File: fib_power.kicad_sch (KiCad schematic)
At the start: 36 parts, among them U201 TLV75718PDBV, U202 TLV75733PDBV, U204 TPS56428DDA, U205 TPS56428DDA

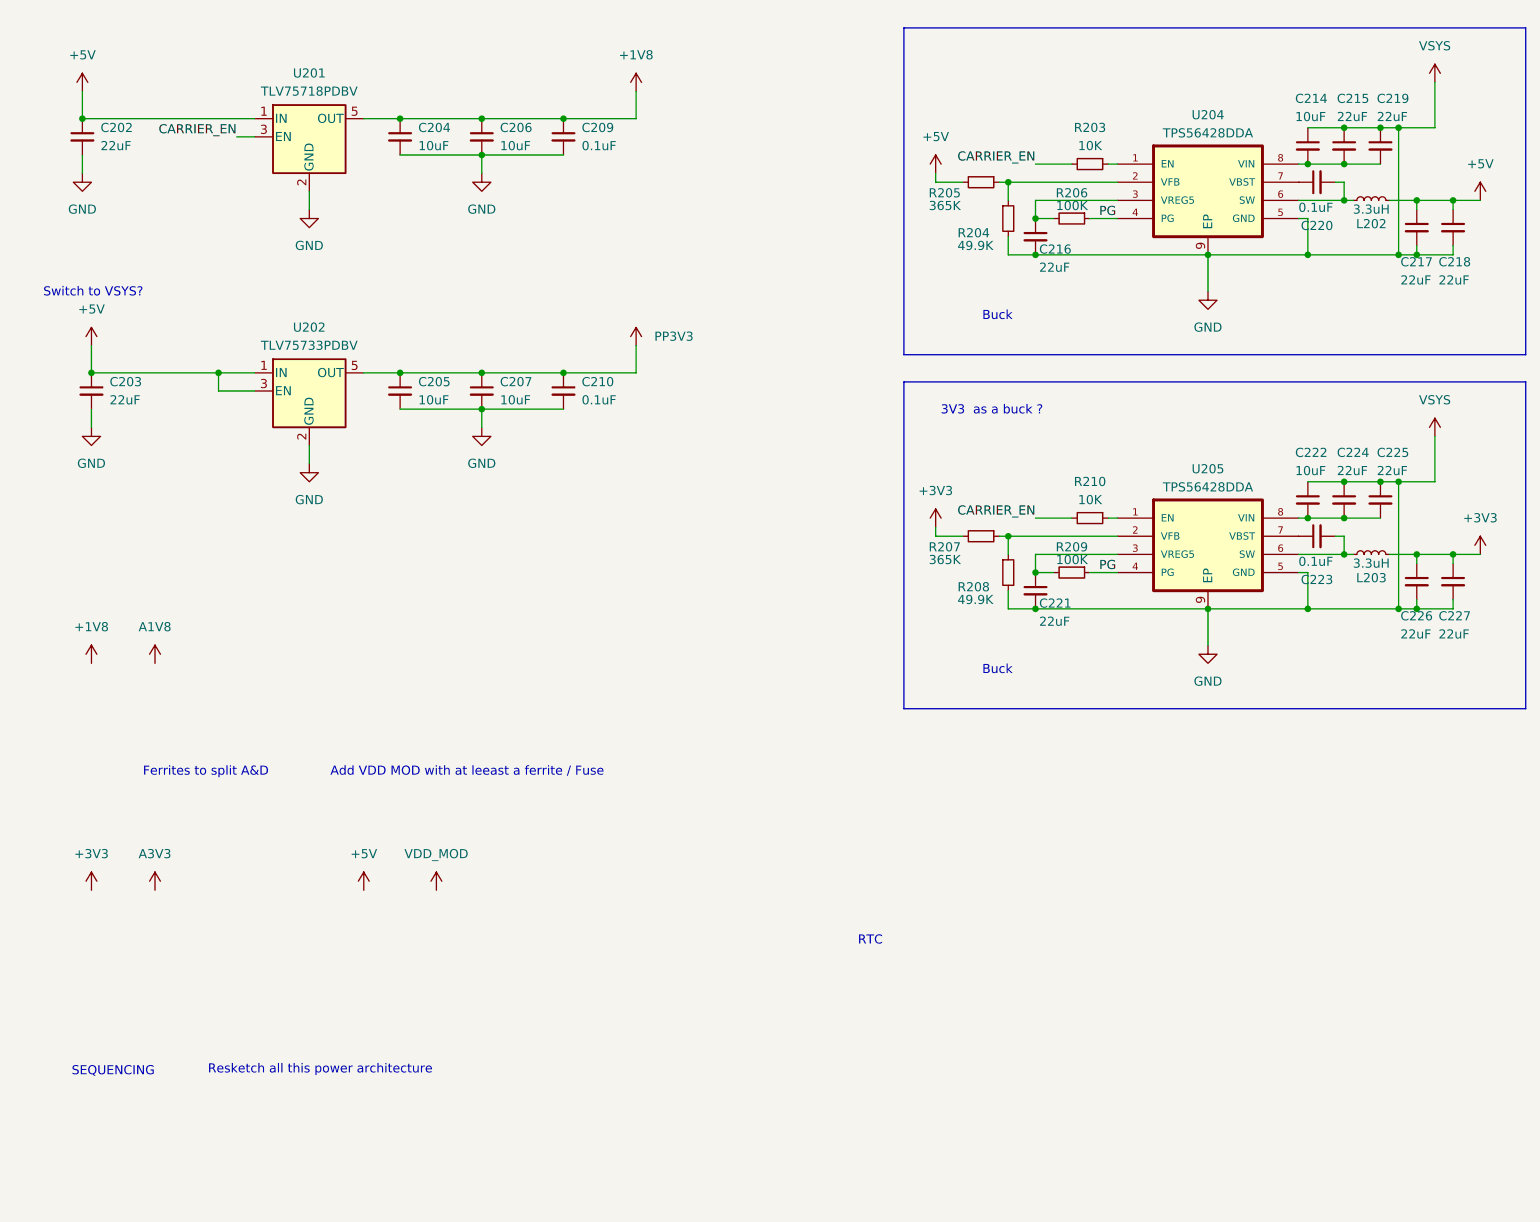
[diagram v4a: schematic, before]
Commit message: started routing the SODIMM, updated connector footprint, started arranging component into sub-areas
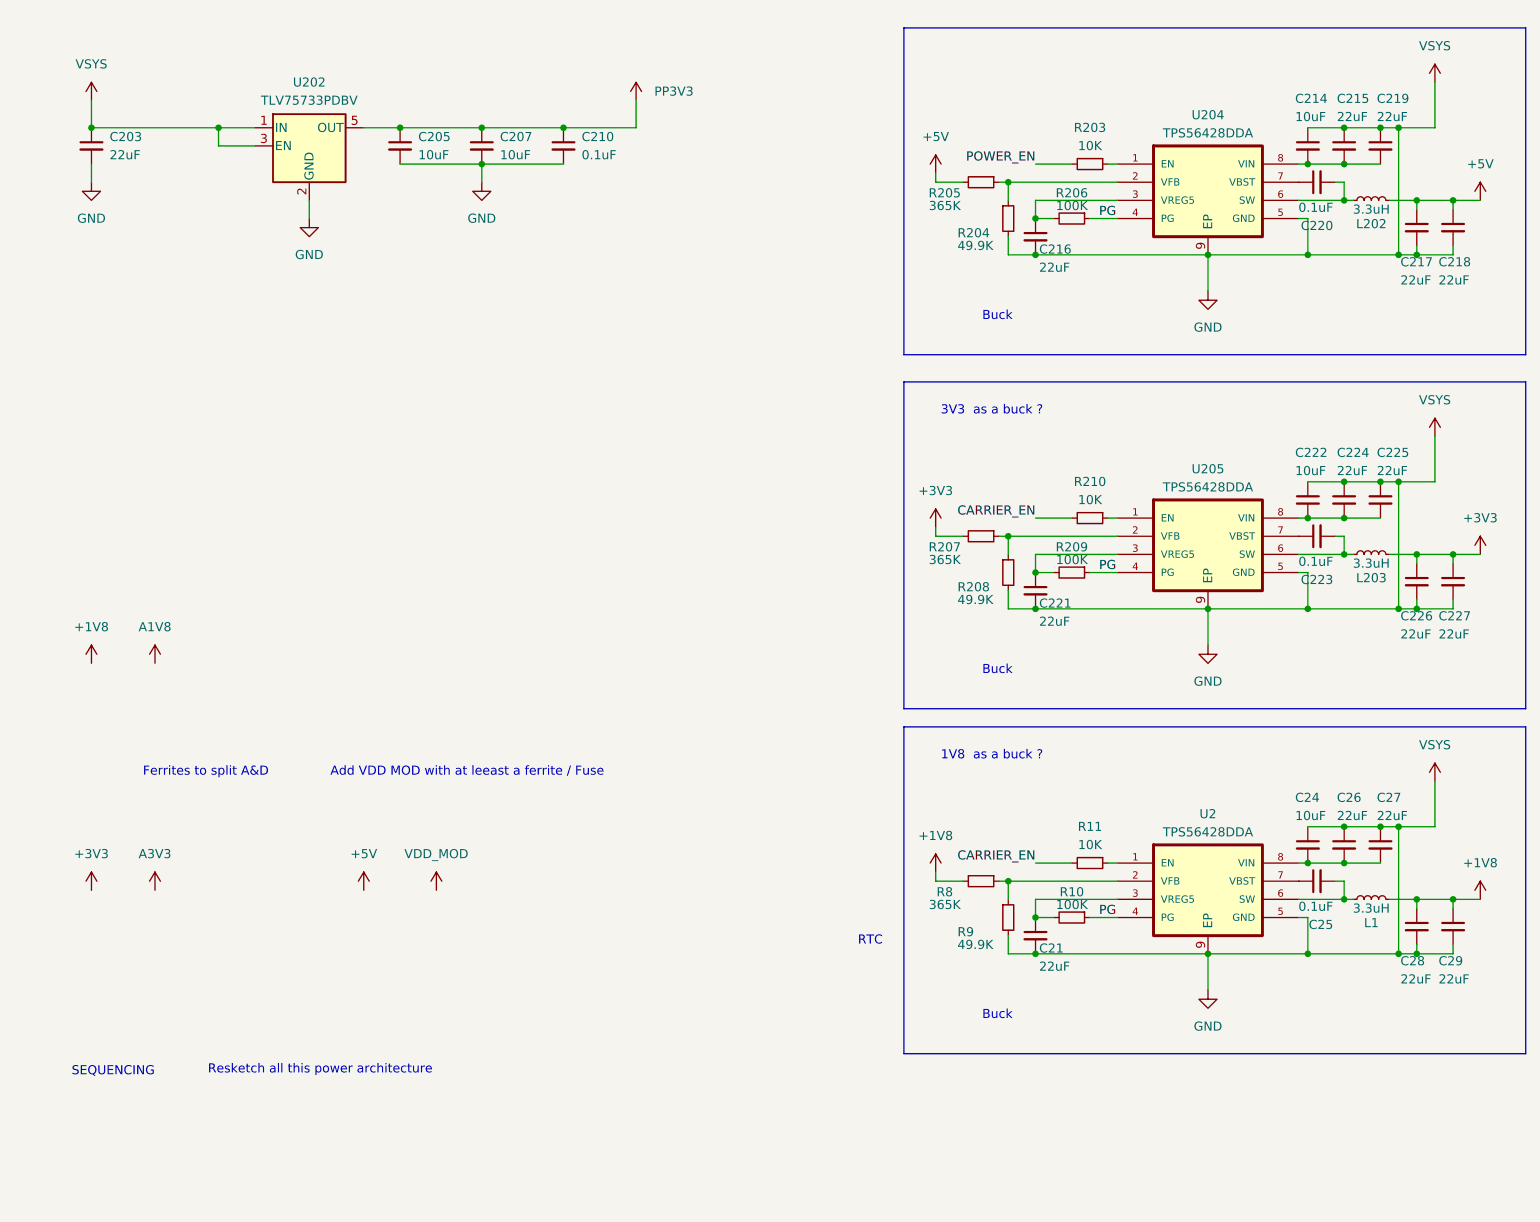
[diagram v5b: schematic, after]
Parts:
- removed C202: 22uF, Capacitor_SMD:C_0805_2012Metric, symbol Device:C_Small
- removed C204, C206: 10uF, Capacitor_SMD:C_0603_1608Metric, symbol Device:C_Small
- removed C209: 0.1uF, Capacitor_SMD:C_0603_1608Metric, symbol Device:C_Small
- removed U201: TLV75718PDBV, Package_TO_SOT_SMD:SOT-23-5, symbol Regulator_Linear:TLV75718PDBV
- added C21, C26, C27, C29: 22uF, Capacitor_SMD:C_0805_2012Metric, symbol Device:C_Small
- added C24: 10uF, Capacitor_SMD:C_0603_1608Metric, symbol Device:C_Small
- added C25: 0.1uF, Capacitor_SMD:C_0805_2012Metric, symbol Device:C_Small
- added C28: 22uF, Capacitor_SMD:C_0603_1608Metric, symbol Device:C_Small
- added L1: 3.3uH, symbol Device:L_Small
- added R10: 100K, Resistor_SMD:R_0603_1608Metric, symbol Device:R_Small
- added R11: 10K, Resistor_SMD:R_0603_1608Metric, symbol Device:R_Small
- added R8: 365K, Resistor_SMD:R_0603_1608Metric, symbol Device:R_Small
- added R9: 49.9K, Resistor_SMD:R_0603_1608Metric, symbol Device:R_Small
- added U2: TPS56428DDA, Fibel2:TPS56428DDA, symbol Fibel2:TPS56428DDA
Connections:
- net +1V8: now also C28.1, C29.1, L1.2, R8.2
- net +5V: no longer C203.1, U202.1 (IN), U202.3 (EN)
- net CARRIER_EN: now also R11.2; no longer R203.2
- net GND: now also C203.1, U202.1 (IN), U202.3 (EN), C21.2, C24.1, C26.1, C27.1, C28.2, C29.2, R9.2, U2.5 (GND), U2.9 (EP)
- net PG: now also R10.1, U2.4 (PG)
- new net: R11.1, U2.1 (EN)
- new net: R8.1, R9.1, U2.2 (VFB)
- new net: C21.1, R10.2, U2.3 (VREG5)
- new net: C25.2, L1.1, U2.6 (SW)
- new net: C25.1, U2.7 (VBST)
- new net: C24.2, C26.2, C27.2, U2.8 (VIN)
- new net POWER_EN: R203.2
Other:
- note added: "1V8 as a buck ?"
- note removed: "Switch to VSYS?"
- moved on the sheet: C203, C205, C207, C210, U202

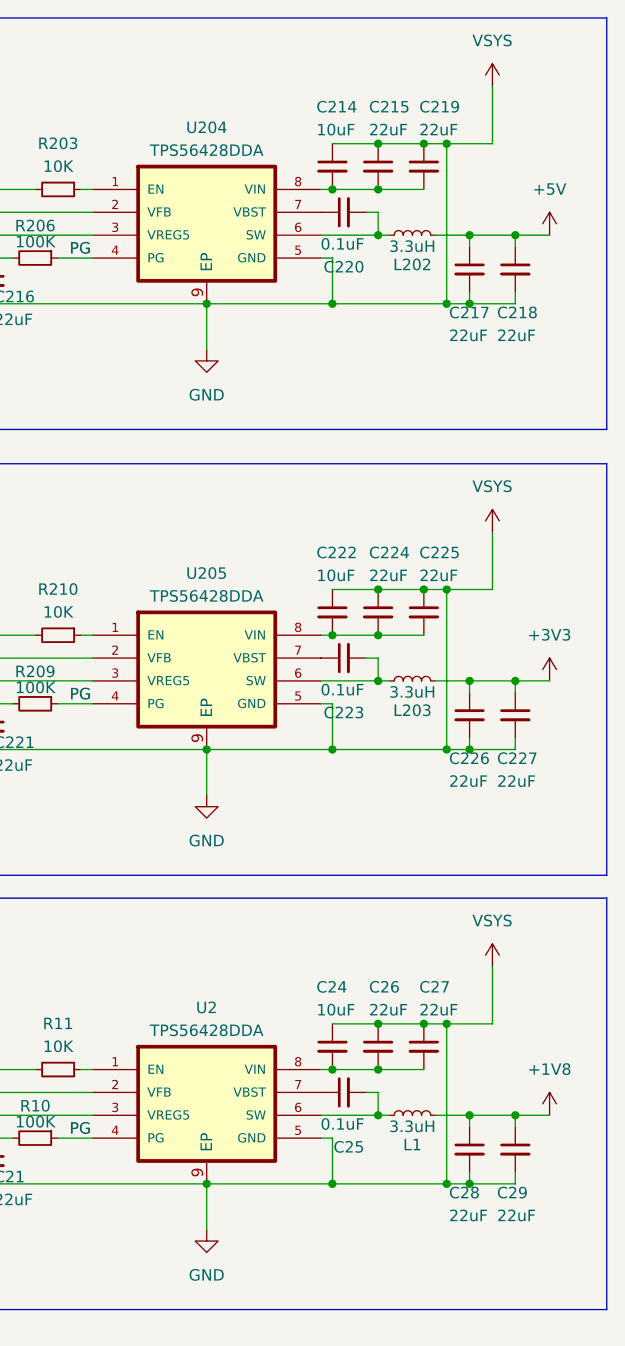
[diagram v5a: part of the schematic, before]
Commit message: implemented most of USB and Power Supplies
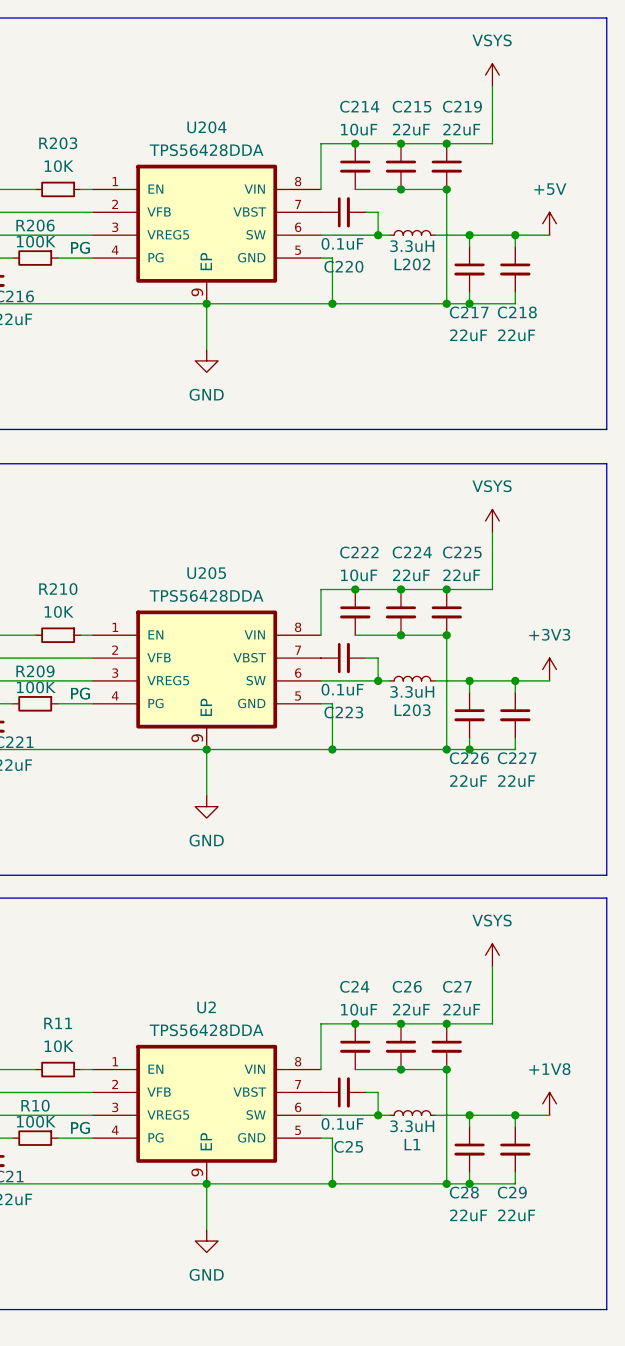
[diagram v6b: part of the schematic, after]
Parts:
- C210: footprint Capacitor_SMD:C_0603_1608Metric -> Capacitor_SMD:C_0402_1005Metric
- C220, C223, C25: footprint Capacitor_SMD:C_0805_2012Metric -> Capacitor_SMD:C_0402_1005Metric
- L202: footprint Resistor_SMD:R_0603_1608Metric -> (none)
- R10, R11, R203, R204, R205, R206, R207, R208, R209, R210, R8, R9: footprint Resistor_SMD:R_0603_1608Metric -> Resistor_SMD:R_0402_1005Metric
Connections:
- net GND: now also C214.2, C215.2, C219.2, C222.2, C224.2, C225.2, C24.2, C26.2, C27.2; no longer C203.1, C214.1, C215.1, C219.1, C222.1, C224.1, C225.1, C24.1, C26.1, C27.1, U202.1 (IN), U202.3 (EN)
- new net VSYS: C203.1, C214.1, C215.1, C219.1, C222.1, C224.1, C225.1, C24.1, C26.1, C27.1, U2.8 (VIN), U202.1 (IN), U202.3 (EN), U204.8 (VIN), U205.8 (VIN)
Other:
- moved on the sheet: C214, C215, C219, C222, C224, C225, C24, C26, C27

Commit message: further optimized placement, finished most of buck array, expanded pcie, added tons of missing footprints, diff pair spacing optimization
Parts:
- L1, L202, L203: footprint (none) -> Inductor_SMD:L_Coilcraft_XAL4030-XXX
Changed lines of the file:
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@@
 			)
 		)
-		(property "Footprint" ""
+		(property "Footprint" "Inductor_SMD:L_Coilcraft_XAL4030-XXX"
 			(at 207.01 39.37 0)
 			(effects
@@
 			)
 		)
-		(property "Footprint" ""
+		(property "Footprint" "Inductor_SMD:L_Coilcraft_XAL4030-XXX"
 			(at 207.01 137.16 0)
 			(effects
@@
 			)
 		)
-		(property "Footprint" ""
+		(property "Footprint" "Inductor_SMD:L_Coilcraft_XAL4030-XXX"
 			(at 207.01 88.9 0)
 			(effects

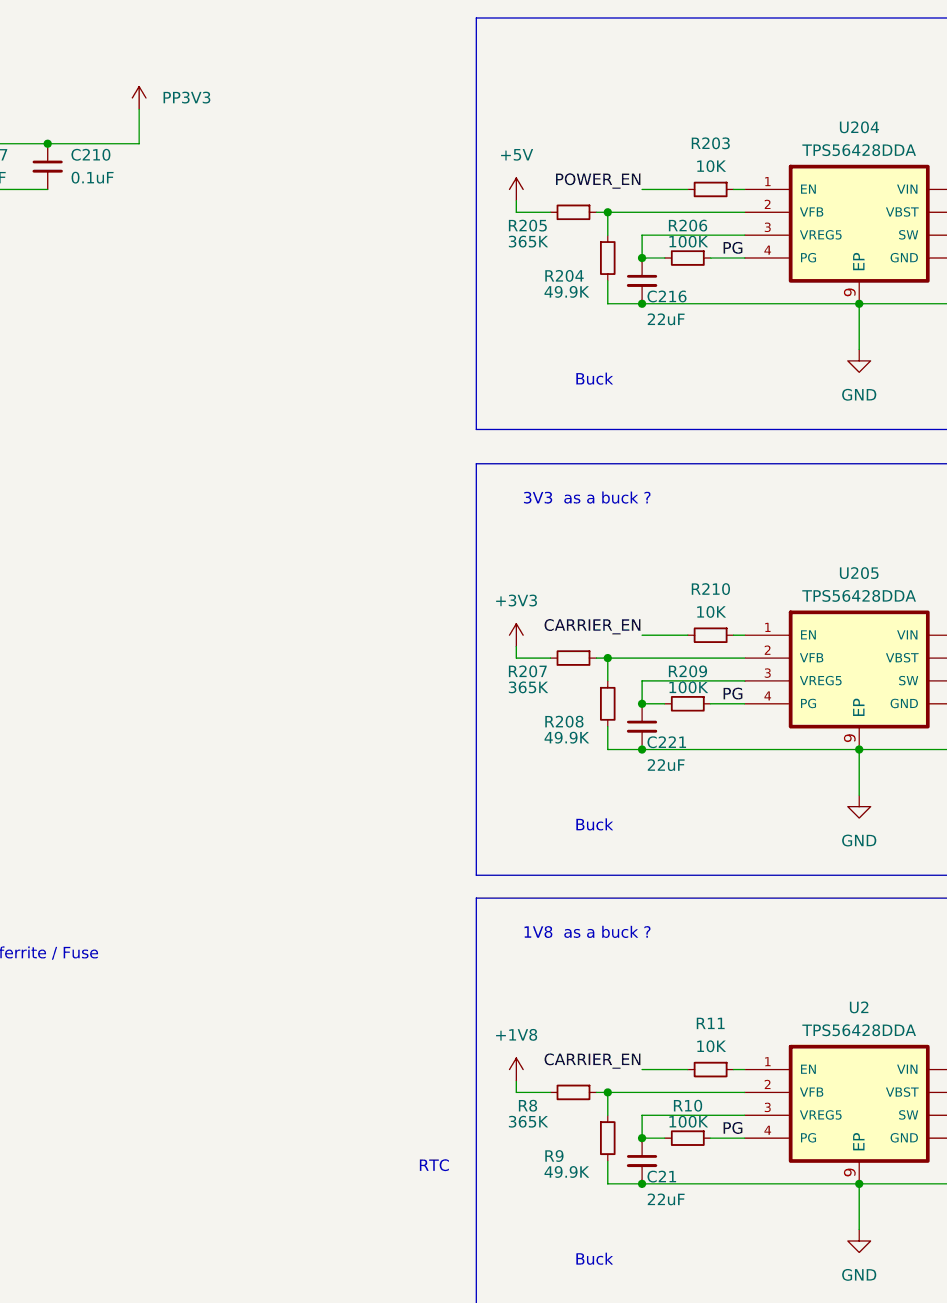
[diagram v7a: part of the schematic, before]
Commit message: 90 percent done with routing. need to go over all schematic pages, double check everything thoroughly, do lengthmatching add any missing footprints, take care of startup, ferrites, audio, eink connectors, 40pin header connections, rtc
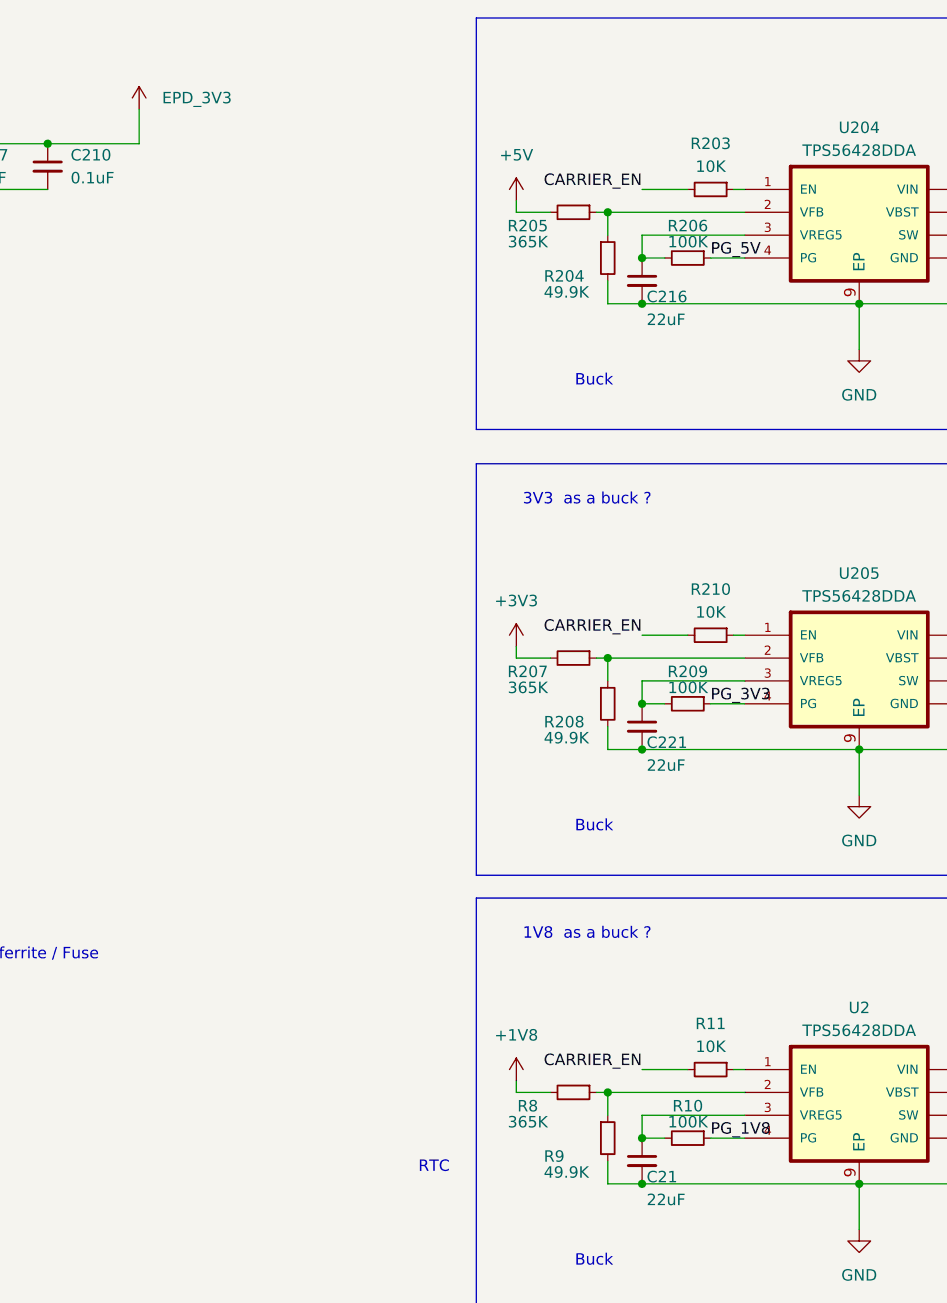
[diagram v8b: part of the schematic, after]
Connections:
- net POWER_EN is gone; now on net CARRIER_EN: R203.2
- removed net PG: R10.1, R206.1, R209.1, U2.4 (PG), U204.4 (PG), U205.4 (PG)
- net PP3V3 renamed EPD_3V3
- new net PG_1V8: R10.1, U2.4 (PG)
- new net PG_3V3: R209.1, U205.4 (PG)
- new net PG_5V: R206.1, U204.4 (PG)
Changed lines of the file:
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@@
 	(wire
 		(pts
+			(xy 167.64 91.44) (xy 171.45 91.44)
+		)
+		(stroke
+			(width 0)
+			(type default)
+		)
+	)
+	(wire
+		(pts
 			(xy 160.02 39.37) (xy 160.02 41.91)
 		)
@@
 	(wire
 		(pts
-			(xy 167.64 91.44) (xy 171.45 91.44)
-		)
-		(stroke
-			(width 0)
-			(type default)
-		)
-	)
-	(wire
-		(pts
 			(xy 200.66 127) (xy 205.74 127)
 		)
@@
 		)
 	)
-	(label "POWER_EN"
+	(label "CARRIER_EN"
 		(at 160.02 34.29 180)
 		(fields_autoplaced yes)
@@
 		)
 	)
-	(label "PG"
-		(at 168.91 41.91 0)
+	(label "PG_5V"
+		(at 167.64 41.91 0)
 		(fields_autoplaced yes)
 		(effects
@@
 		)
 	)
-	(label "PG"
-		(at 168.91 91.44 0)
+	(label "PG_3V3"
+		(at 167.64 91.44 0)
 		(fields_autoplaced yes)
 		(effects
@@
 		)
 	)
-	(label "PG"
-		(at 168.91 139.7 0)
+	(label "PG_1V8"
+		(at 167.64 139.7 0)
 		(fields_autoplaced yes)
 		(effects
@@
 			)
 		)
-		(property "Value" "PP3V3"
+		(property "Value" "EPD_3V3"
 			(at 106.68 24.1299 0)
 			(effects
